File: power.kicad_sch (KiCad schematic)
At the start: 29 parts, among them U3 AP2112K-3.3, U4 LM317_TO-252, U5 LMR36520FADDA

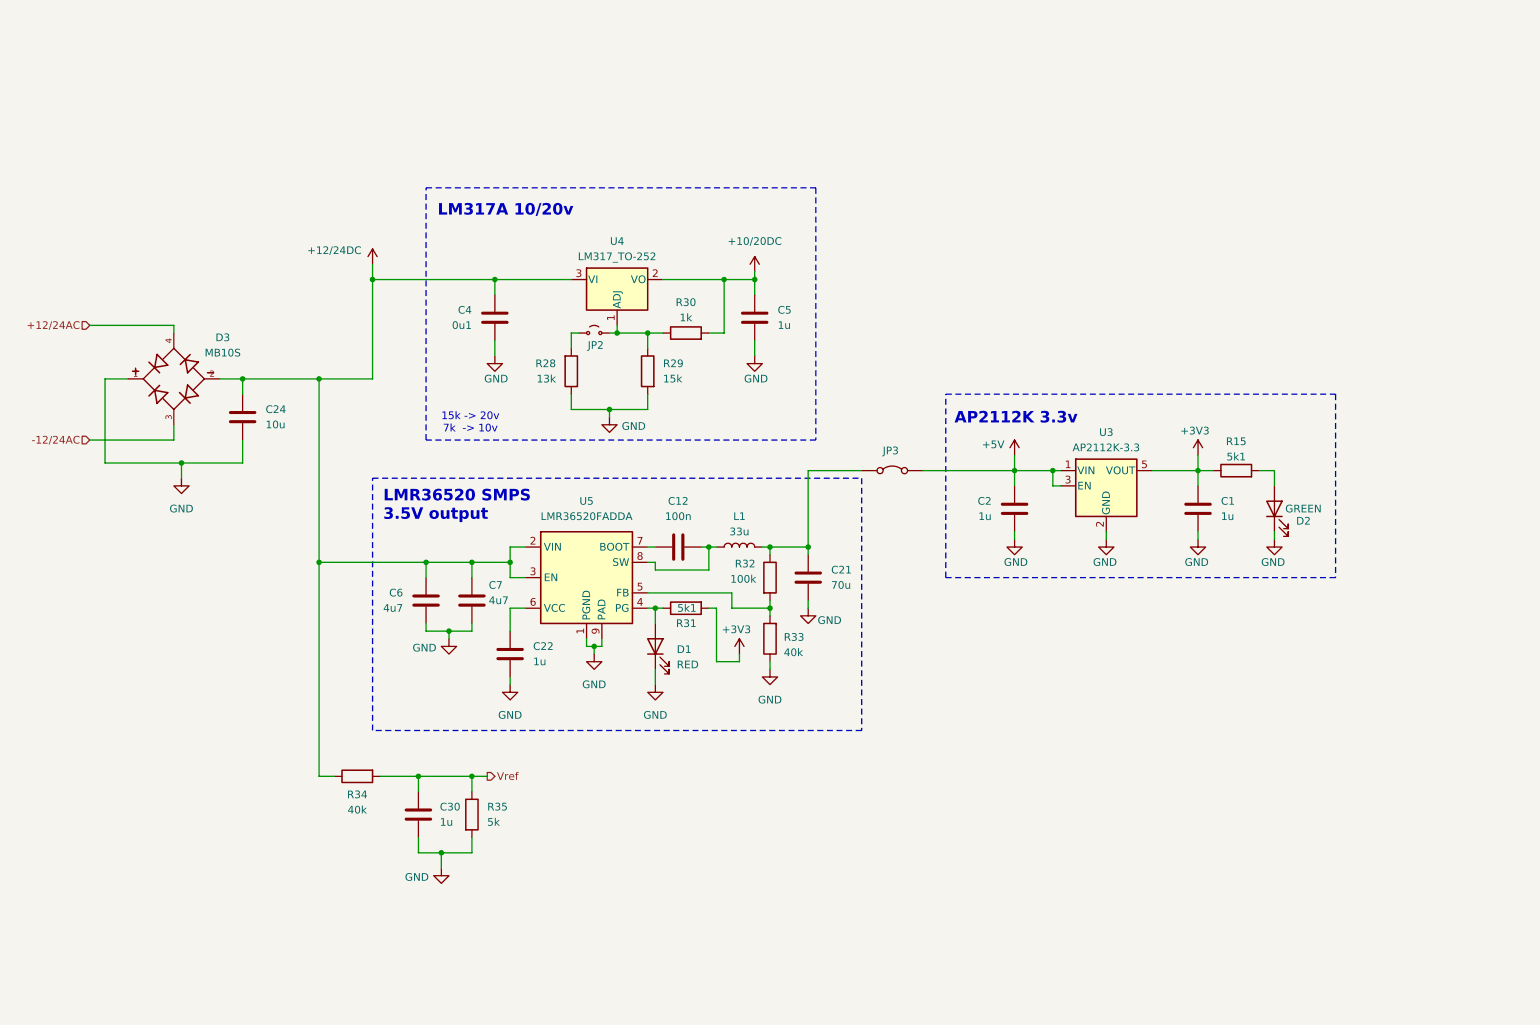
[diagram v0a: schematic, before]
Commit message: schem: add CJ431 24v & 12v voltage references
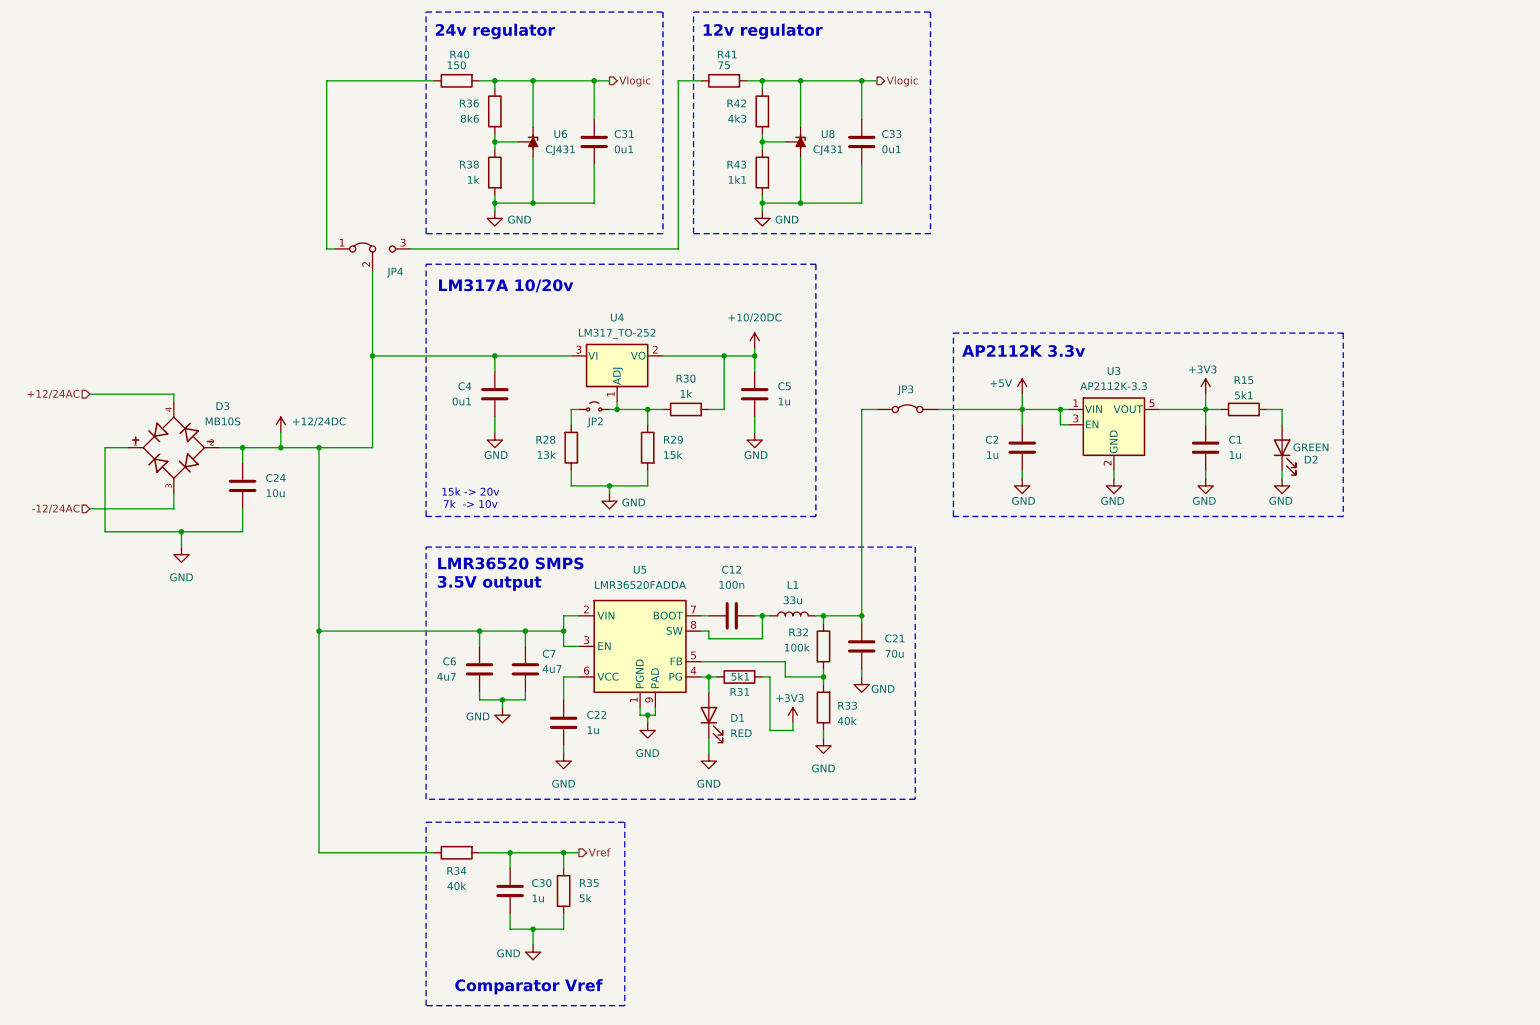
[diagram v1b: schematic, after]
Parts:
- added C31, C33: 0u1, symbol Device:C
- added JP4: Jumper_3_Bridged12, symbol Jumper:Jumper_3_Bridged12
- added R36: 8k6, symbol Device:R
- added R38: 1k, symbol Device:R
- added R40: 150, symbol Device:R
- added R41: 75, symbol Device:R
- added R42: 4k3, symbol Device:R
- added R43: 1k1, symbol Device:R
- added U6, U8: CJ431, Package_TO_SOT_SMD:SOT-23, symbol Pers:CJ431
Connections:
- net +12/24DC: now also JP4.2 (C)
- net GND: now also C31.2, C33.2, R38.2, R43.2, U6.3 (A), U8.3 (A)
- new net: JP4.3 (B), R41.1
- new net: R36.2, R38.1, U6.1 (REF)
- new net: R42.2, R43.1, U8.1 (REF)
- new net: JP4.1 (A), R40.1
- new net Vlogic: C31.1, C33.1, R36.1, R40.2, R41.2, R42.1, U6.2 (K), U8.2 (K)
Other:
- note added: "12v regulator"
- note added: "24v regulator"
- note added: "Comparator Vref"
- moved on the sheet: C1, C12, C2, C21, C22, C24, C30, C4, C5, C6, C7, D1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

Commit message: schem: add LMR36520 24v smps
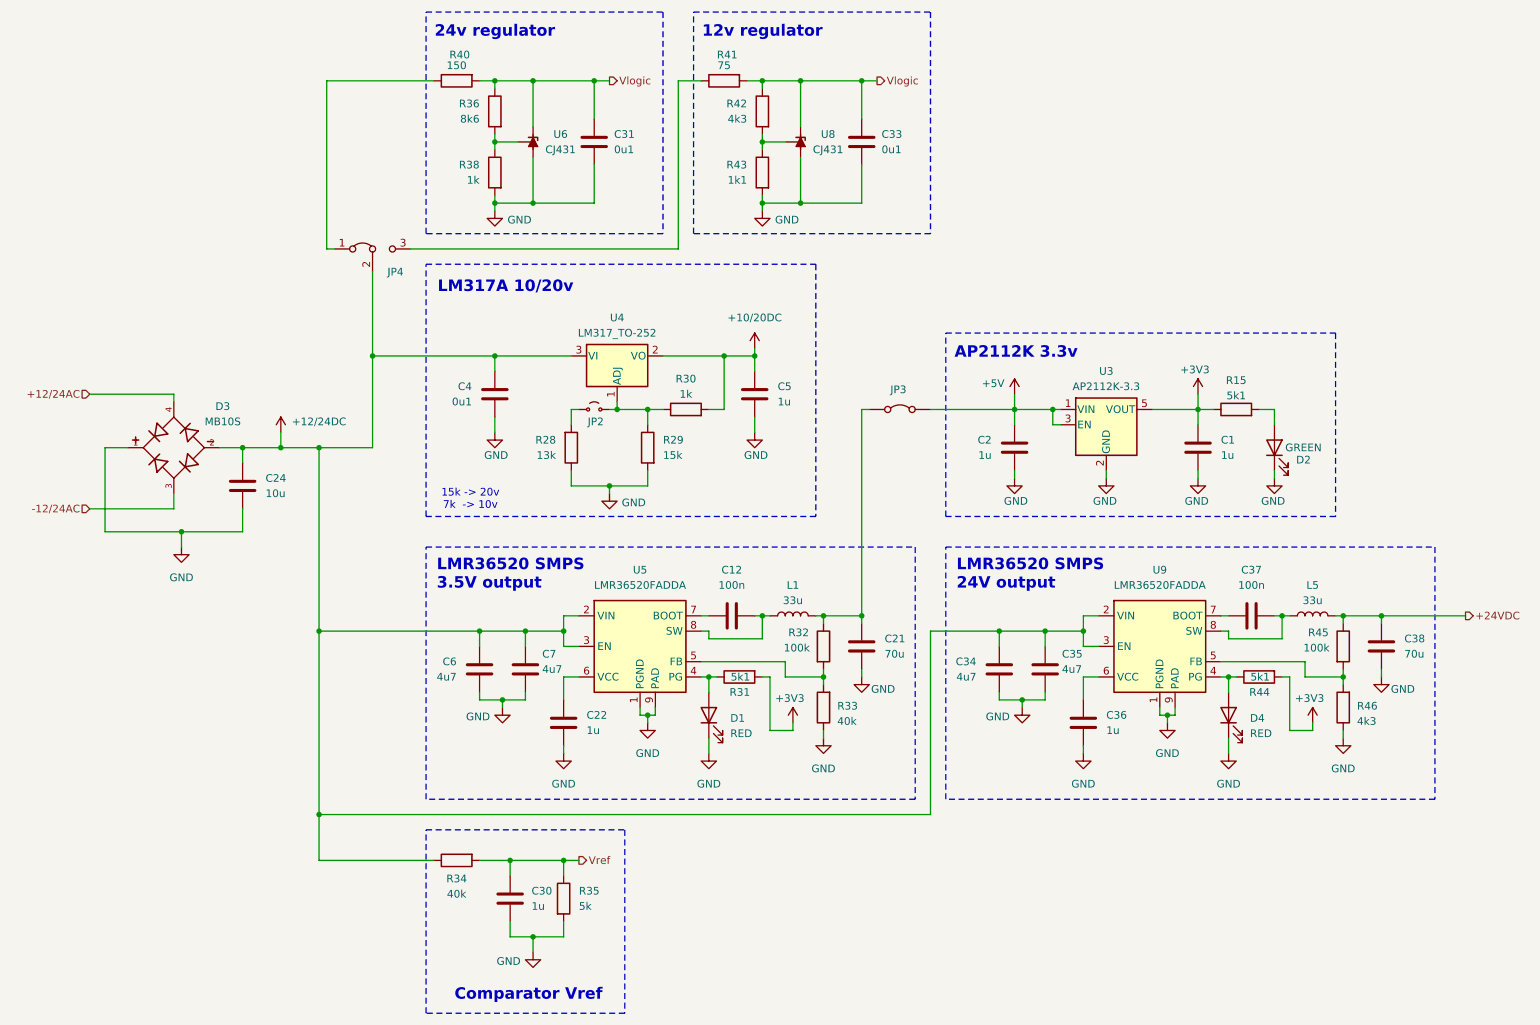
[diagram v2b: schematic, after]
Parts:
- added C34, C35: 4u7, symbol Device:C
- added C36: 1u, symbol Device:C
- added C37: 100n, symbol Device:C
- added C38: 70u, symbol Device:C
- added D4: RED, symbol Device:LED
- added L5: 33u, symbol Device:L
- added R44: 5k1, symbol Device:R
- added R45: 100k, symbol Device:R
- added R46: 4k3, symbol Device:R
- added U9: LMR36520FADDA, Package_SO:Texas_HTSOP-8-1EP_3.9x4.9mm_P1.27mm_EP2.95x4.9mm_Mask2.4x3.1mm_ThermalVias, symbol Pers:LMR36520FADDA
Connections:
- net +12/24DC: now also C34.1, C35.1, U9.2 (VIN), U9.3 (EN)
- net +3V3: now also R44.2
- net GND: now also C34.2, C35.2, C36.2, C38.1, D4.1 (K), R46.1, U9.1 (PGND), U9.9 (PAD)
- new net: D4.2 (A), R44.1, U9.4 (PG)
- new net: R45.2, R46.2, U9.5 (FB)
- new net: C36.1, U9.6 (VCC)
- new net: C37.2, U9.7 (BOOT)
- new net: C37.1, L5.1, U9.8 (SW)
- new net +24VDC: C38.2, L5.2, R45.1
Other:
- note added: "LMR36520 SMPS 24V output"
- moved on the sheet: C1, C2, C30, D2, JP3, R15, R34, R35, U3

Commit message: schem: add power test points
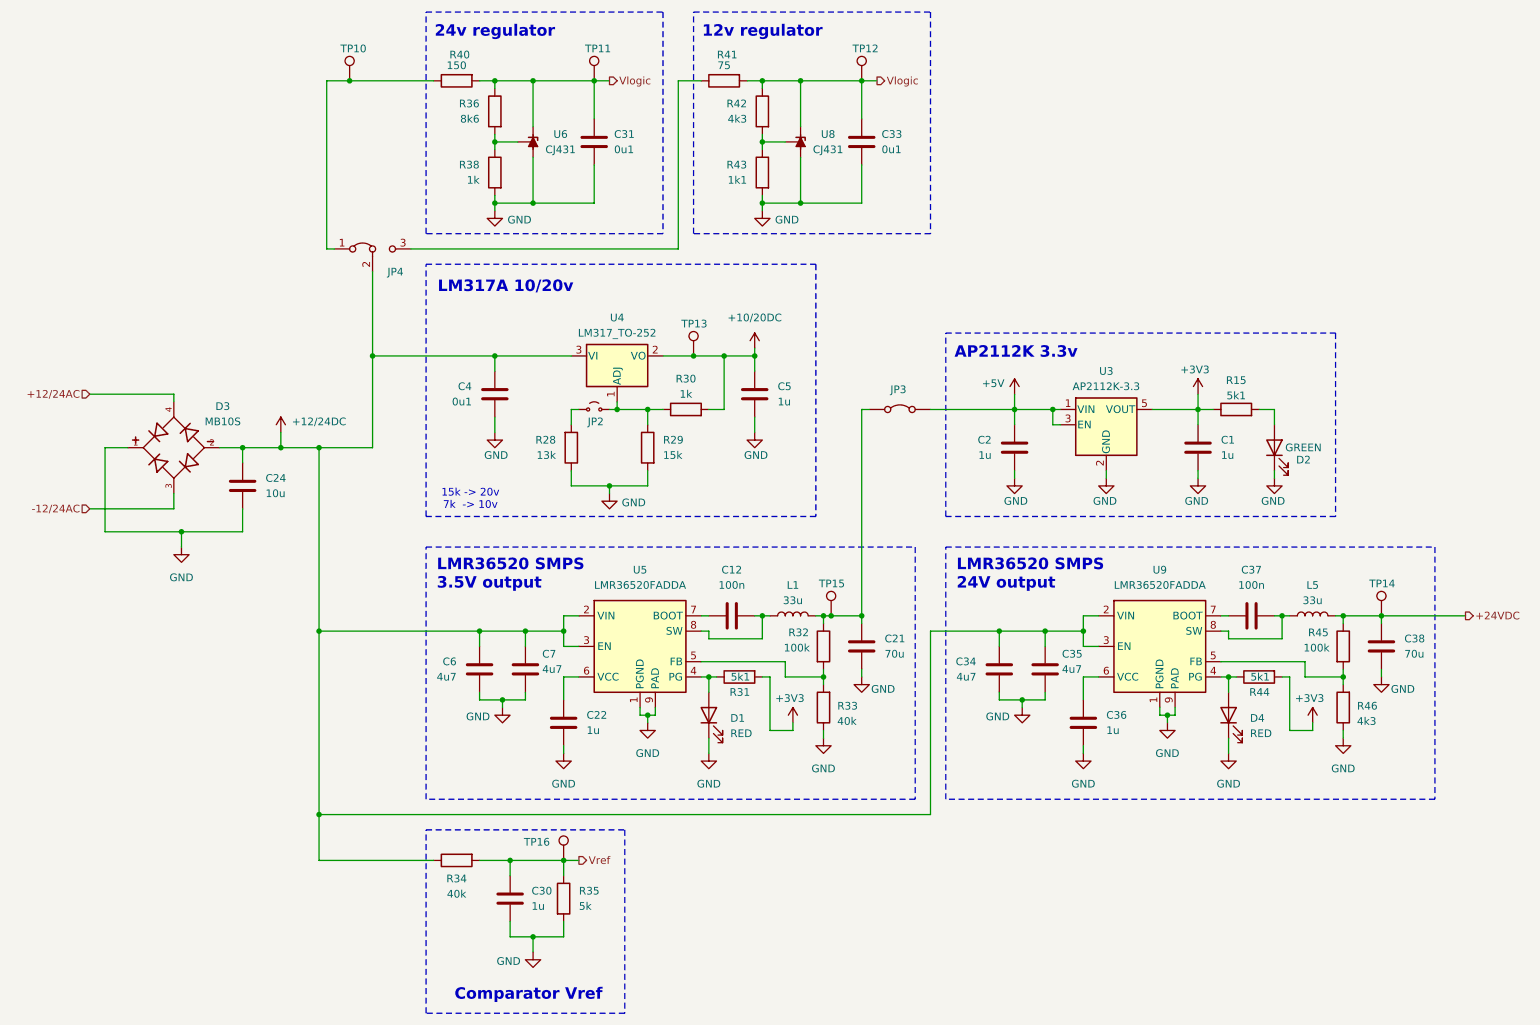
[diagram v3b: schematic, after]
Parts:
- added TP10, TP11, TP12, TP13, TP14, TP15, TP16: TestPoint, symbol Connector:TestPoint
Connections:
- net +10/20DC: now also TP13.1
- net +24VDC: now also TP14.1
- net Vlogic: now also TP11.1, TP12.1
- net Vref: now also TP16.1
- net at C21.2, JP3.1 (A), L1.2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: now also TP15.1
- net at JP4.1 (A), R40.1: now also TP10.1

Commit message: schem: add sheet titles
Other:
- company: (none) -> Rémi Ait-Younes
- title: (none) -> Power section
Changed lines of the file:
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@@
 	(generator_version "9.0")
 	(paper "A4")
+	(title_block
+		(title "Power section")
+		(date "2025-09-26")
+		(rev "01")
+		(company "Rémi Ait-Younes")
+	)
 	(rectangle
 		(start 91.44 161.29)

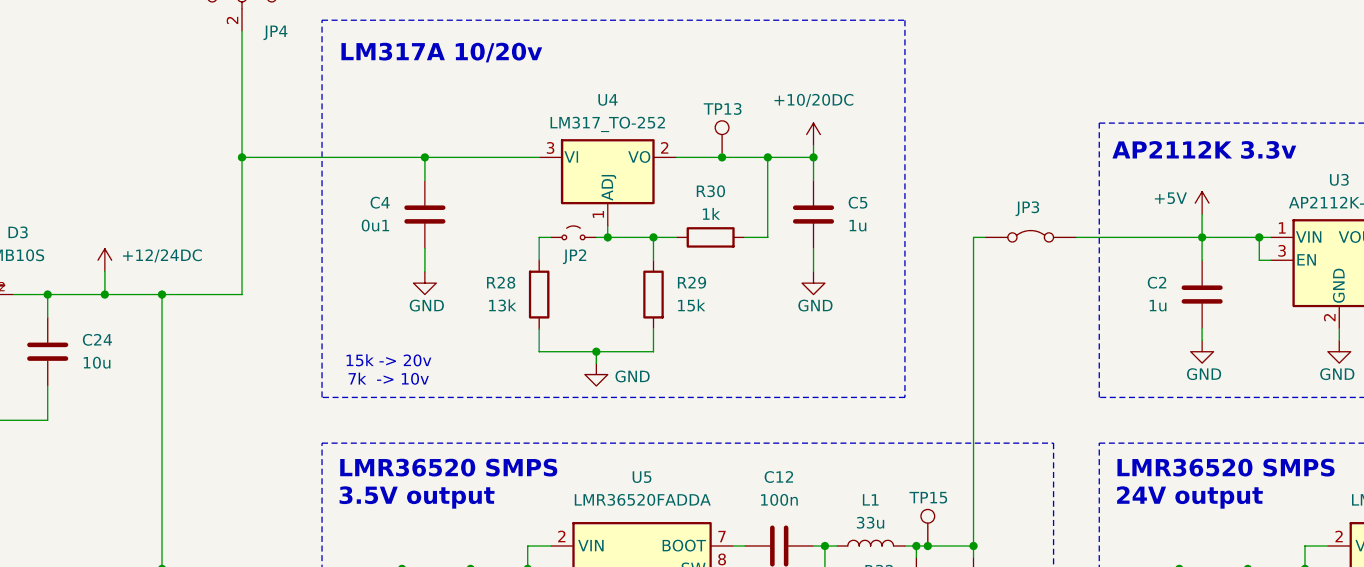
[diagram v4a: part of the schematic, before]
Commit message: schem: fix erc
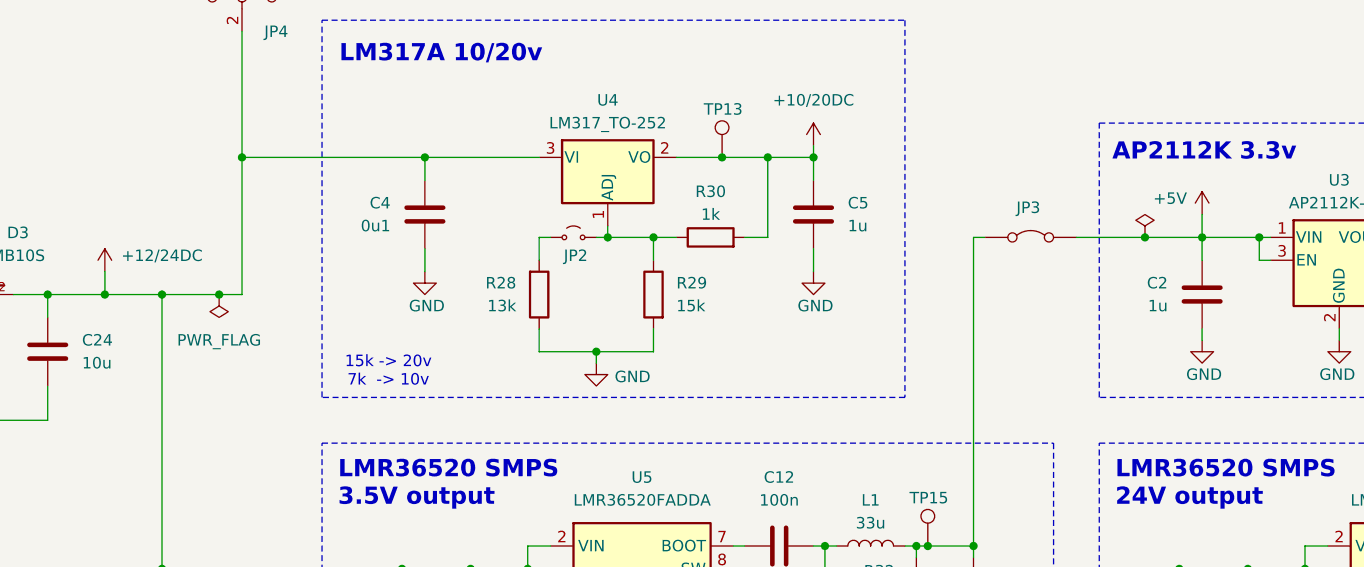
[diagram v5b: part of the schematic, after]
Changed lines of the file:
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@@
 	)
 	(junction
+		(at 182.88 91.44)
+		(diameter 0)
+		(color 0 0 0 0)
+	)
+	(junction
 		(at 104.14 139.7)
 		(diameter 0)
@@
 	)
 	(junction
+		(at 80.01 97.79)
+		(diameter 0)
+		(color 0 0 0 0)
+	)
+	(junction
 		(at 200.66 128.27)
 		(diameter 0)
@@
 	(wire
 		(pts
-			(xy 73.66 97.79) (xy 82.55 97.79)
+			(xy 73.66 97.79) (xy 80.01 97.79)
 		)
 		(stroke
@@
 	(wire
 		(pts
+			(xy 182.88 91.44) (xy 189.23 91.44)
+		)
+		(stroke
+			(width 0)
+			(type default)
+		)
+	)
+	(wire
+		(pts
 			(xy 203.2 125.73) (xy 200.66 125.73)
 		)
@@
 	(wire
 		(pts
-			(xy 175.26 91.44) (xy 189.23 91.44)
+			(xy 175.26 91.44) (xy 182.88 91.44)
 		)
 		(stroke
@@
 	(wire
 		(pts
+			(xy 80.01 97.79) (xy 82.55 97.79)
+		)
+		(stroke
+			(width 0)
+			(type default)
+		)
+	)
+	(wire
+		(pts
 			(xy 102.87 57.15) (xy 102.87 55.88)
 		)
@@
 	)
 	(symbol
+		(lib_id "power:PWR_FLAG")
+		(at 80.01 97.79 180)
+		(unit 1)
+		(exclude_from_sim no)
+		(in_bom yes)
+		(on_board yes)
+		(dnp no)
+		(fields_autoplaced yes)
+		(property "Reference" "#FLG05"
+			(at 80.01 99.695 0)
+			(effects
+				(font
+					(size 1.27 1.27)
+				)
+				(hide yes)
+			)
+		)
+		(property "Value" "PWR_FLAG"
+			(at 80.01 102.87 0)
+			(effects
+				(font
+					(size 1.27 1.27)
+				)
+			)
+		)
+		(property "Footprint" ""
+			(at 80.01 97.79 0)
+			(effects
+				(font
+					(size 1.27 1.27)
+				)
+				(hide yes)
+			)
+		)
+		(property "Datasheet" "~"
+			(at 80.01 97.79 0)
+			(effects
+				(font
+					(size 1.27 1.27)
+				)
+				(hide yes)
+			)
+		)
+		(property "Description" "Special symbol for telling ERC where power comes from"
+			(at 80.01 97.79 0)
+			(effects
+				(font
+					(size 1.27 1.27)
+				)
+				(hide yes)
+			)
+		)
+		(pin "1"
+		)
+		(instances
+			(project ""
+				(path "/f6edeef8-7fa0-4f55-9ad8-145372f41e3e/4befa429-10a8-402a-b91d-1560a39651d5"
+					(reference "#FLG05")
+					(unit 1)
+				)
+			)
+		)
+	)
+	(symbol
 		(lib_id "Device:R")
 		(at 102.87 41.91 0)
@@
 					(unit 1)
 				)
+			)
+		)
+	)
+	(symbol
+		(lib_id "power:PWR_FLAG")
+		(at 182.88 91.44 0)
+		(unit 1)
+		(exclude_from_sim no)
+		(in_bom yes)
+		(on_board yes)
+		(dnp no)
+		(fields_autoplaced yes)
+		(property "Reference" "#FLG04"
+			(at 182.88 89.535 0)
+			(effects
+				(font
+					(size 1.27 1.27)
+				)
+				(hide yes)
+			)
+		)
+		(property "Value" "PWR_FLAG"
+			(at 182.88 86.36 0)
+			(effects
+				(font
+					(size 1.27 1.27)
+				)
+				(hide yes)
+			)
+		)
+		(property "Footprint" ""
+			(at 182.88 91.44 0)
+			(effects
+				(font
+					(size 1.27 1.27)
+				)
+				(hide yes)
+			)
+		)
+		(property "Datasheet" "~"
+			(at 182.88 91.44 0)
+			(effects
+				(font
+					(size 1.27 1.27)
+				)
+				(hide yes)
+			)
+		)
+		(property "Description" "Special symbol for telling ERC where power comes from"
+			(at 182.88 91.44 0)
+			(effects
+				(font
+					(size 1.27 1.27)
+				)
+				(hide yes)
+			)
+		)
+		(pin "1"
+		)
+		(instances
+			(project ""
+				(path "/f6edeef8-7fa0-4f55-9ad8-145372f41e3e/4befa429-10a8-402a-b91d-1560a39651d5"
+					(reference "#FLG04")
+					(unit 1)
+				)
